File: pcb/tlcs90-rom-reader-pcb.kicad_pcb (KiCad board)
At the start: 2 copper layers, 111.8 x 121.9 mm, 59 parts, among them J1 Conn_01x04, J2 Conn_Coaxial_Power, Q1 Q_NPN_ECB, SW1 SW_SPDT, SW2 SW_SPDT, SW3 SW_Push, SW4 SW_SPDT, U1 TMP90C840AN, U10 74LS08, U11 74LS04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

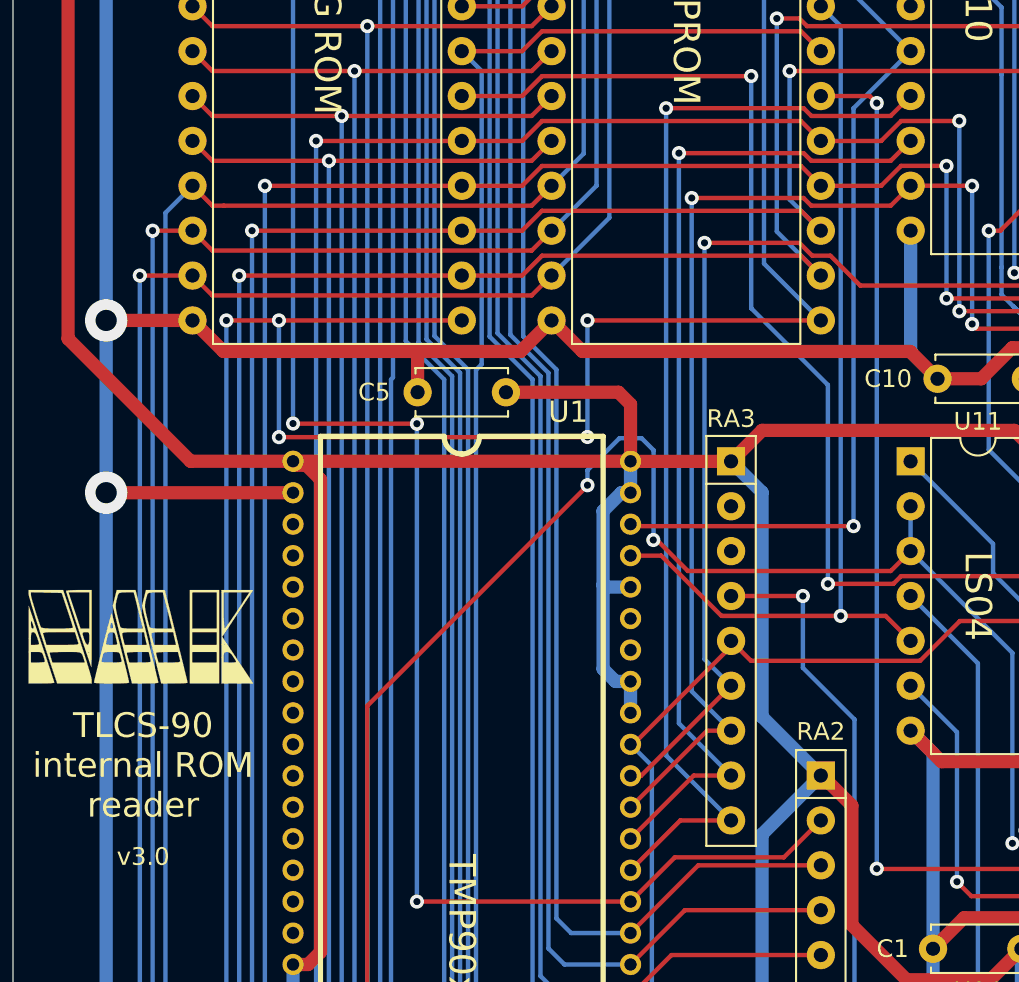
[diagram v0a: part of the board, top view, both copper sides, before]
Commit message: new 3.1: added pull-up resistors to /RD and /WR signals
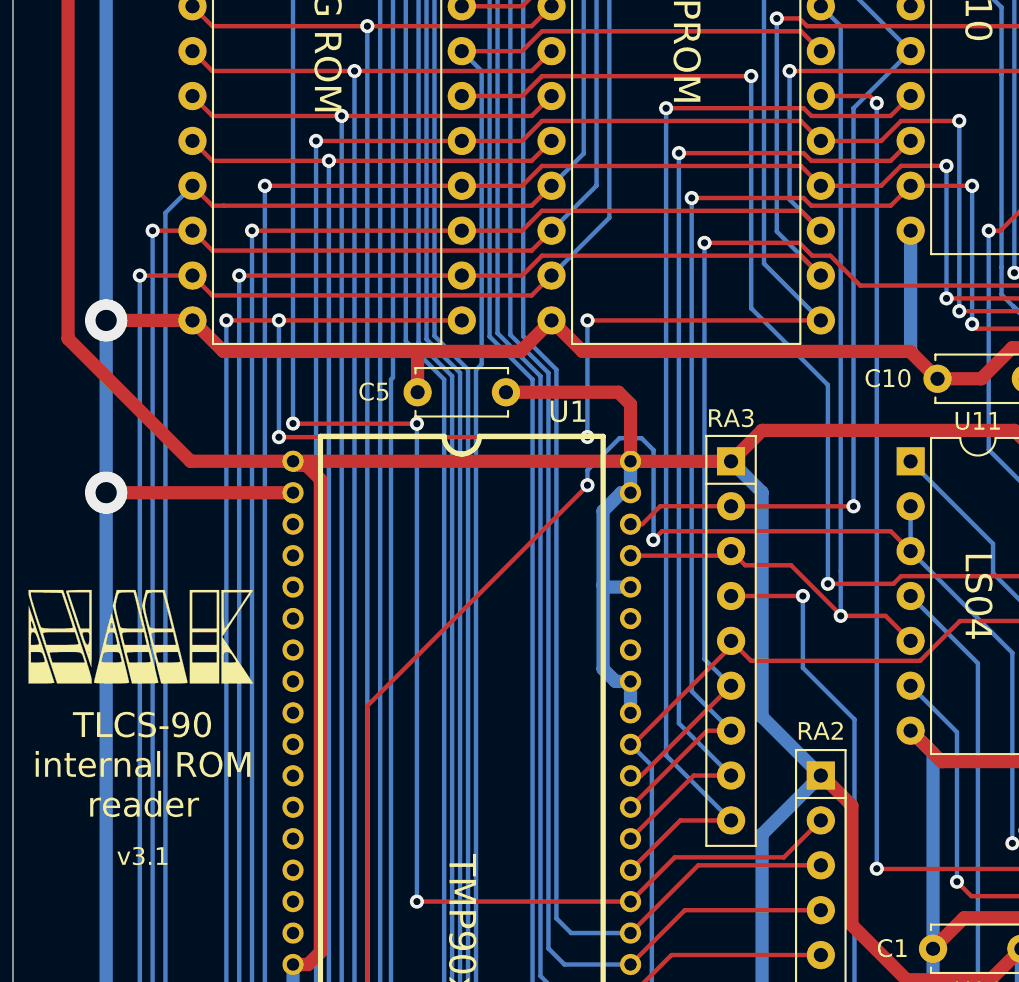
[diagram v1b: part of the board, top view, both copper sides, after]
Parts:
- renumbered L2 to ee
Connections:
- RA3 pad 2: (no net) -> ~WR
- RA3 pad 3: (no net) -> ~RD
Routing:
- net ~WR: track 58.2 -> 57.6 mm
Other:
- board text added: "v3.1"
- board text removed: "v3.0"

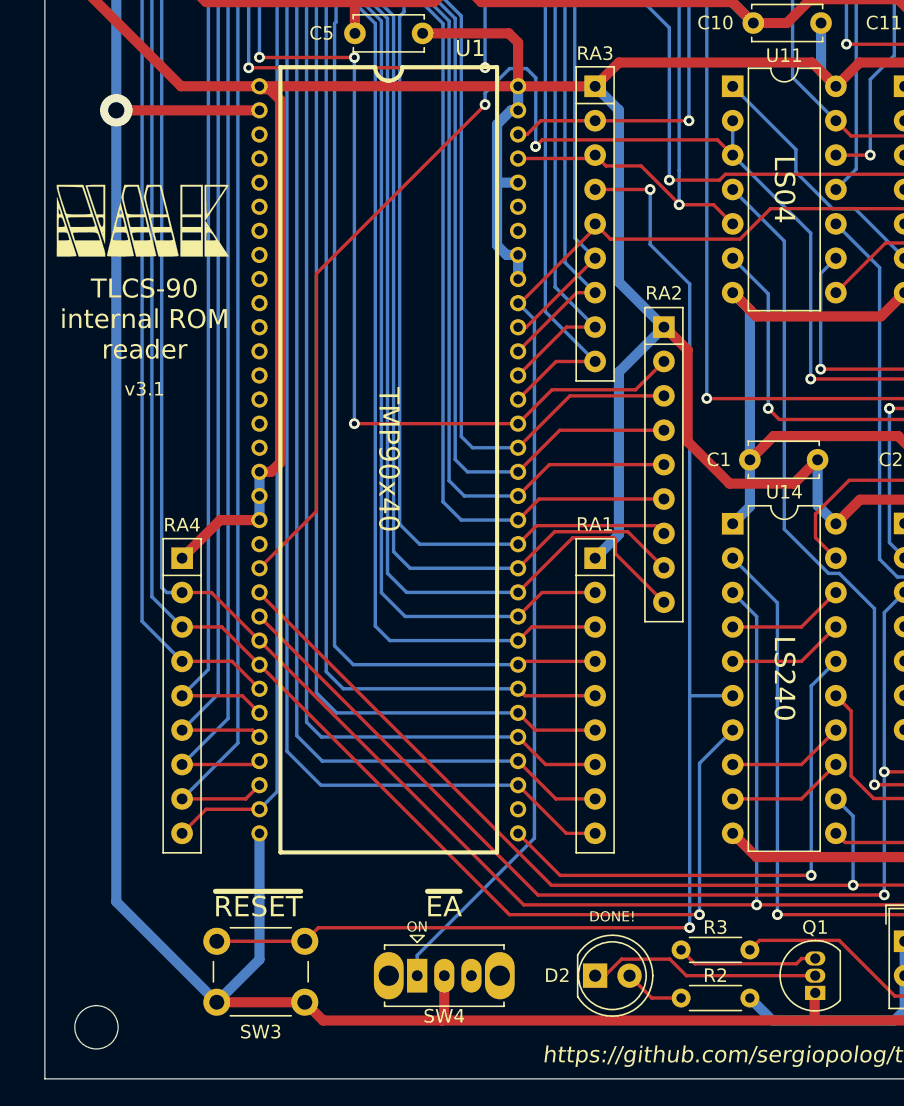
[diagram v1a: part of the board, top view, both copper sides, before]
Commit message: update pcb: add selector to set Pull-up or Pull-down resistors on address and data buses
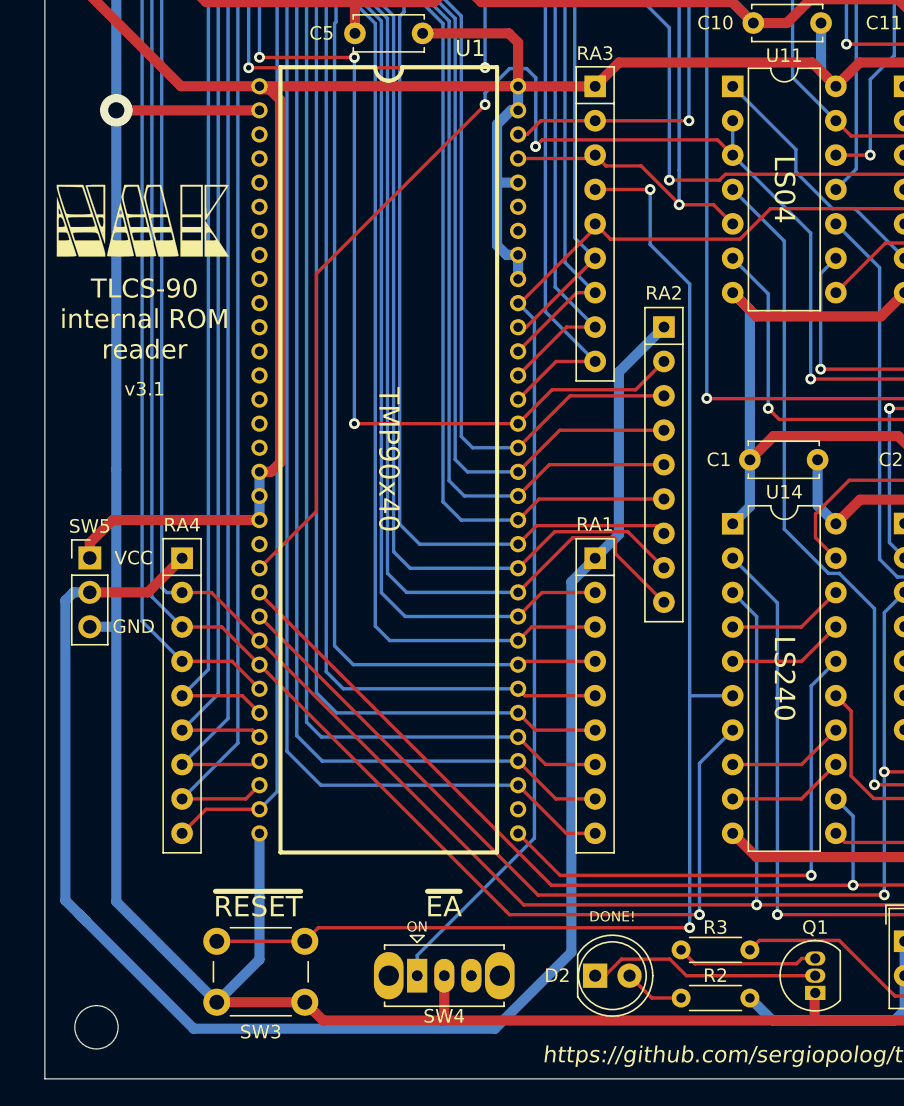
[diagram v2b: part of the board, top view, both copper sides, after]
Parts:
- added SW5: PinHeader, Connector_PinHeader_2.54mm:PinHeader_1x03_P2.54mm_Vertical, F.Cu at (82.1, 116.5)
- renumbered ee to L2
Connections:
- RA1 pad 1: VCC -> Net-(RA1-Pad1)
- RA2 pad 1: VCC -> Net-(RA1-Pad1)
- RA4 pad 1: VCC -> Net-(RA1-Pad1)
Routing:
- net Net-(RA1-Pad1): track 0.00 -> 125.4 mm
- net VCC: track 663.9 -> 611.5 mm
- net GND: track 860.3 -> 862.3 mm
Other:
- board text added: "VCC"
